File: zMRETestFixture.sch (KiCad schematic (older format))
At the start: 210 parts, among them J1 Conn_01x01, J10 Conn_01x01, J11 Conn_01x01, J2 Conn_01x01, J3 Conn_01x01_Female, J4 Conn_01x01_Female, J5 Conn_01x01, J6 Conn_01x01, J7 Conn_01x01, J8 Conn_01x01, J9 Conn_02x05_Counter_Clockwise, SW1 SW_Push, SW2 SW_Push, U1 molex_48pin_MRE

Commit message: Updated https://github.com/rusefi/hw_microRusEfi/issues/163
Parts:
- removed R57: 5k, rusefi_lib:SM0805_jumper, symbol Device:R
- removed R59: 470k, rusefi_lib:SM0805_jumper, symbol Device:R
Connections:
- wire segments 303 -> 302
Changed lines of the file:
@@
 Wire Wire Line
 	5900 2575 5900 1575
-Text Label 10725 2600 2    60   ~ 12
-5V1
-Text Label 10675 1500 2    60   ~ 12
-5V2
 Wire Wire Line
 	11525 2600 11625 2600
-$Comp
-L Device:R R59
-U 1 1 5F5B6BED
-P 11625 1650
-F 0 "R59" V 11725 1575 50  0000 L CNN
-F 1 "470k" V 11625 1650 50  0000 C CNN
-F 2 "rusefi_lib:SM0805_jumper" V 11555 1650 50  0001 C CNN
-F 3 "~" H 11625 1650 50  0001 C CNN
-F 4 "" H 3300 -4275 50  0001 C CNN "Manufacturer"
-F 5 "" H 3300 -4275 50  0001 C CNN "Part #"
-F 6 "" H 3300 -4275 50  0001 C CNN "VEND"
-F 7 "" H 3300 -4275 50  0001 C CNN "VEND#"
-F 8 "C17709" H 11625 1650 50  0001 C CNN "LCSC"
-	1    11625 1650
-	-1   0    0    1
-$EndComp
 $Comp
 L power:GND #PWR07
 U 1 1 5F5B882A
-P 11625 1875
-F 0 "#PWR07" H 11625 1625 50  0001 C CNN
-F 1 "GND" H 11630 1702 50  0000 C CNN
-F 2 "" H 11625 1875 50  0001 C CNN
-F 3 "" H 11625 1875 50  0001 C CNN
-	1    11625 1875
+P 11075 1575
+F 0 "#PWR07" H 11075 1325 50  0001 C CNN
+F 1 "GND" H 11080 1402 50  0000 C CNN
+F 2 "" H 11075 1575 50  0001 C CNN
+F 3 "" H 11075 1575 50  0001 C CNN
+	1    11075 1575
 	1    0    0    -1
 $EndComp
 Text Label 11625 1500 0    60   ~ 12
 CAM_SENSOR
-Wire Wire Line
-	10825 2600 10725 2600
-Wire Wire Line
-	10775 1500 10675 1500
 Wire Wire Line
 	9550 1575 9550 1950
@@
 Connection ~ 6425 5225
 Wire Wire Line
-	11625 1800 11625 1875
+	11075 1500 11075 1575
 Wire Wire Line
 	11625 1500 11475 1500
-Connection ~ 11625 1500
-$Comp
-L Device:R R60
-U 1 1 5F8A0C67
-P 11625 2750
-F 0 "R60" V 11725 2675 50  0000 L CNN
-F 1 "470k" V 11625 2750 50  0000 C CNN
-F 2 "rusefi_lib:SM0805_jumper" V 11555 2750 50  0001 C CNN
-F 3 "~" H 11625 2750 50  0001 C CNN
-F 4 "" H 3300 -3175 50  0001 C CNN "Manufacturer"
-F 5 "" H 3300 -3175 50  0001 C CNN "Part #"
-F 6 "" H 3300 -3175 50  0001 C CNN "VEND"
-F 7 "" H 3300 -3175 50  0001 C CNN "VEND#"
-F 8 "C17709" H 11625 2750 50  0001 C CNN "LCSC"
-	1    11625 2750
-	-1   0    0    1
-$EndComp
-$Comp
-L power:GND #PWR08
-U 1 1 5F8A5FD9
-P 11625 2975
-F 0 "#PWR08" H 11625 2725 50  0001 C CNN
-F 1 "GND" H 11630 2802 50  0000 C CNN
-F 2 "" H 11625 2975 50  0001 C CNN
-F 3 "" H 11625 2975 50  0001 C CNN
-	1    11625 2975
-	1    0    0    -1
-$EndComp
-Wire Wire Line
-	11625 2900 11625 2975
-Connection ~ 11625 2600
 Text Label 11625 2600 0    60   ~ 12
 CRNK+
-$Comp
-L Device:R R58
-U 1 1 5F96A20E
-P 10975 2600
-F 0 "R58" V 11025 2725 50  0000 L CNN
-F 1 "5k" V 10975 2600 50  0000 C CNN
-F 2 "rusefi_lib:SM0805_jumper" V 10905 2600 50  0001 C CNN
-F 3 "~" H 10975 2600 50  0001 C CNN
-F 4 "" H 2650 -3325 50  0001 C CNN "Manufacturer"
-F 5 "" H 2650 -3325 50  0001 C CNN "Part #"
-F 6 "" H 2650 -3325 50  0001 C CNN "VEND"
-F 7 "" H 2650 -3325 50  0001 C CNN "VEND#"
-F 8 "C17677" H 10975 2600 50  0001 C CNN "LCSC"
-	1    10975 2600
-	0    -1   1    0
-$EndComp
-$Comp
-L Device:R R57
-U 1 1 5F9948F0
-P 10925 1500
-F 0 "R57" V 10975 1625 50  0000 L CNN
-F 1 "5k" V 10925 1500 50  0000 C CNN
-F 2 "rusefi_lib:SM0805_jumper" V 10855 1500 50  0001 C CNN
-F 3 "~" H 10925 1500 50  0001 C CNN
-F 4 "" H 2600 -4425 50  0001 C CNN "Manufacturer"
-F 5 "" H 2600 -4425 50  0001 C CNN "Part #"
-F 6 "" H 2600 -4425 50  0001 C CNN "VEND"
-F 7 "" H 2600 -4425 50  0001 C CNN "VEND#"
-F 8 "C17677" H 10925 1500 50  0001 C CNN "LCSC"
-	1    10925 1500
-	0    -1   1    0
-$EndComp
 $Comp
 L Connector:Conn_01x01_Female J3
@@
 	0    1    1    0
 $EndComp
+Wire Wire Line
+	11625 2900 11625 2975
+$Comp
+L power:GND #PWR08
+U 1 1 5F8A5FD9
+P 11625 2975
+F 0 "#PWR08" H 11625 2725 50  0001 C CNN
+F 1 "GND" H 11630 2802 50  0000 C CNN
+F 2 "" H 11625 2975 50  0001 C CNN
+F 3 "" H 11625 2975 50  0001 C CNN
+	1    11625 2975
+	1    0    0    -1
+$EndComp
+Connection ~ 11625 2600
+$Comp
+L Device:R R60
+U 1 1 5F8A0C67
+P 11625 2750
+F 0 "R60" V 11725 2675 50  0000 L CNN
+F 1 "470k" V 11625 2750 50  0000 C CNN
+F 2 "rusefi_lib:SM0805_jumper" V 11555 2750 50  0001 C CNN
+F 3 "~" H 11625 2750 50  0001 C CNN
+F 4 "" H 3300 -3175 50  0001 C CNN "Manufacturer"
+F 5 "" H 3300 -3175 50  0001 C CNN "Part #"
+F 6 "" H 3300 -3175 50  0001 C CNN "VEND"
+F 7 "" H 3300 -3175 50  0001 C CNN "VEND#"
+F 8 "C17709" H 11625 2750 50  0001 C CNN "LCSC"
+	1    11625 2750
+	-1   0    0    1
+$EndComp
+Wire Wire Line
+	10825 2600 10725 2600
+Text Label 10725 2600 2    60   ~ 12
+5V1
+$Comp
+L Device:R R58
+U 1 1 5F96A20E
+P 10975 2600
+F 0 "R58" V 11025 2725 50  0000 L CNN
+F 1 "5k" V 10975 2600 50  0000 C CNN
+F 2 "rusefi_lib:SM0805_jumper" V 10905 2600 50  0001 C CNN
+F 3 "~" H 10975 2600 50  0001 C CNN
+F 4 "" H 2650 -3325 50  0001 C CNN "Manufacturer"
+F 5 "" H 2650 -3325 50  0001 C CNN "Part #"
+F 6 "" H 2650 -3325 50  0001 C CNN "VEND"
+F 7 "" H 2650 -3325 50  0001 C CNN "VEND#"
+F 8 "C17677" H 10975 2600 50  0001 C CNN "LCSC"
+	1    10975 2600
+	0    -1   1    0
+$EndComp
 $EndSCHEMATC

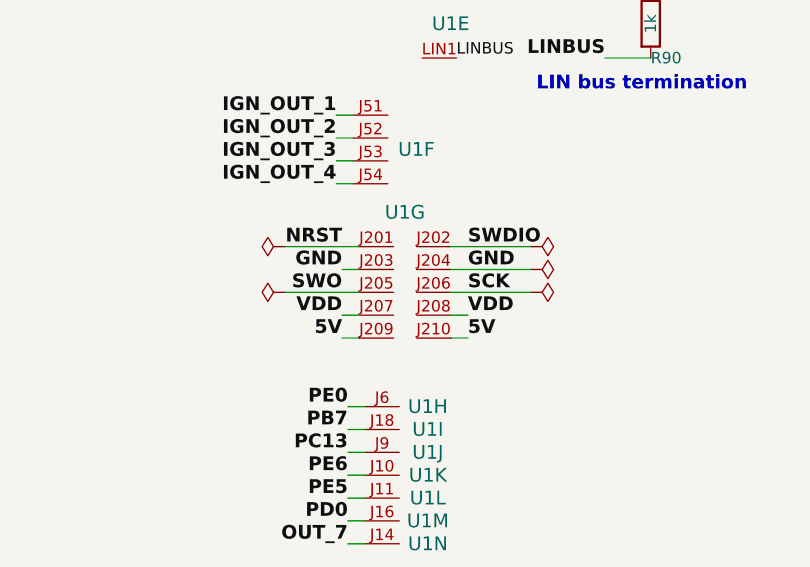
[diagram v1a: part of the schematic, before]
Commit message: Fixed flipped J2 per https://github.com/rusefi/hw_microRusEfi/issues/179
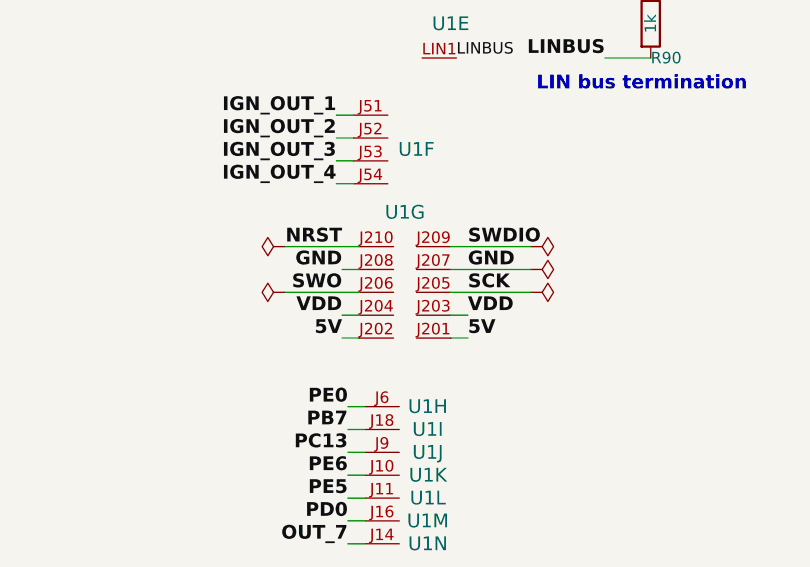
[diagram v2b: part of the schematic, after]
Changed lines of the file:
@@
 Sheet 1 1
 Title "zMRETestFixture"
-Date "2020-05-14"
-Rev "R0.1"
+Date "2020-07-08"
+Rev "R0.2"
 Comp "rusEFI.com"
 Comment1 ""
@@
 L rusefi_Molex_MRE_Connector:molex_48pin_MRE U1
 U 7 1 5EE5179C
-P 13825 3900
-F 0 "U1" H 14725 4250 60  0000 C CNN
-F 1 "molex_48pin_MRE" V 15006 4305 60  0001 C CNN
-F 2 "rusefi_lib:Molex_48_MRE" H 13825 3900 60  0001 C CNN
-F 3 "" H 13825 3900 60  0001 C CNN
-F 4 "MOLEX" H 6075 1775 50  0001 C CNN "Manufacturer"
-F 5 "500762-0481" H 6075 1775 50  0001 C CNN "Part #"
-F 6 "DIGI" H 6075 1775 50  0001 C CNN "VEND"
-F 7 "WM4430-ND" H 6075 1775 50  0001 C CNN "VEND#"
-	7    13825 3900
-	1    0    0    -1
-$EndComp
-$Comp
+P 15625 3900
+F 0 "U1" H 16525 3550 60  0000 C CNN
+F 1 "molex_48pin_MRE" V 16806 4305 60  0001 C CNN
+F 2 "rusefi_lib:Molex_48_MRE" H 15625 3900 60  0001 C CNN
+F 3 "" H 15625 3900 60  0001 C CNN
+F 4 "MOLEX" H 7875 1775 50  0001 C CNN "Manufacturer"
+F 5 "500762-0481" H 7875 1775 50  0001 C CNN "Part #"
+F 6 "DIGI" H 7875 1775 50  0001 C CNN "VEND"
+F 7 "WM4430-ND" H 7875 1775 50  0001 C CNN "VEND#"
+	7    15625 3900
+	-1   0    0    1
+$EndComp
+$Comp

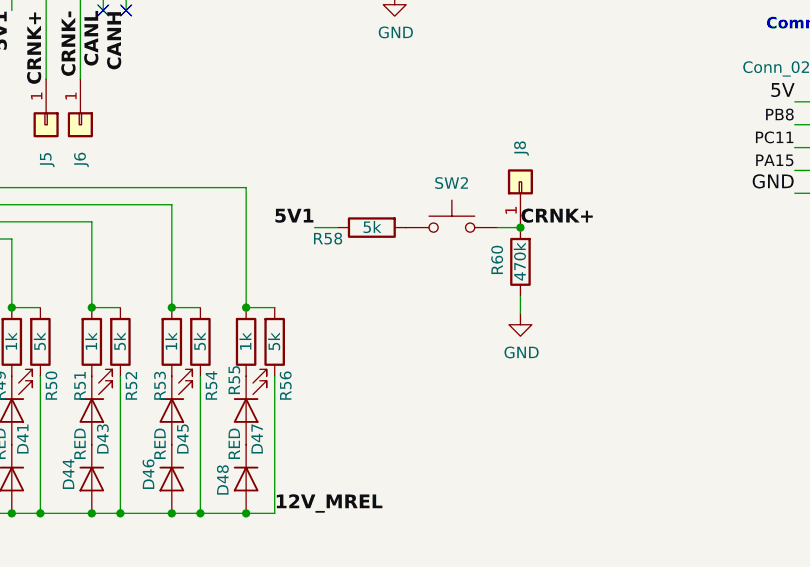
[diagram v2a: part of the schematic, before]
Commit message: Bumped silk to to R0.2 and changed CRANK per https://github.com/rusefi/hw_microRusEfi/issues/177
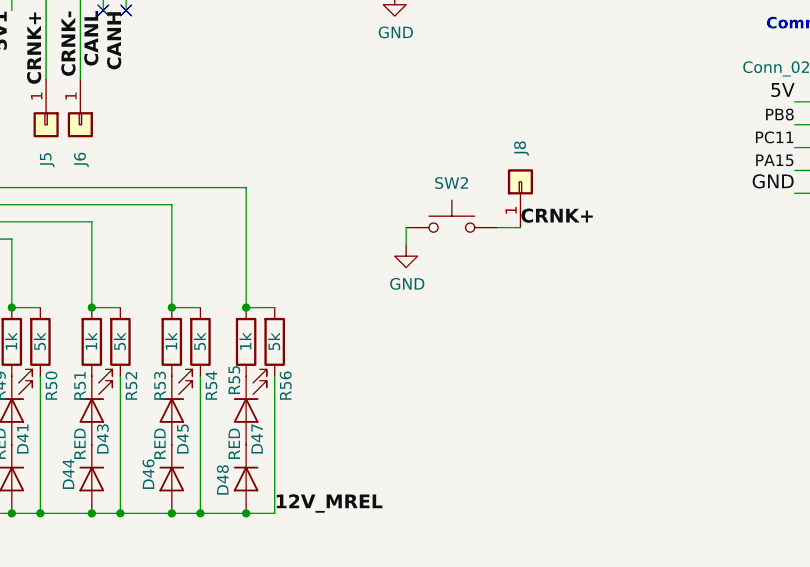
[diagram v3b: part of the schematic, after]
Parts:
- removed R58: 5k, rusefi_lib:SM0805_jumper, symbol Device:R
- removed R60: 470k, rusefi_lib:SM0805_jumper, symbol Device:R
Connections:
- wire segments 302 -> 301
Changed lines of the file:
@@
 $EndComp
 Wire Wire Line
-	11625 2900 11625 2975
+	11125 2600 11125 2675
 $Comp
 L power:GND #PWR08
 U 1 1 5F8A5FD9
-P 11625 2975
-F 0 "#PWR08" H 11625 2725 50  0001 C CNN
-F 1 "GND" H 11630 2802 50  0000 C CNN
-F 2 "" H 11625 2975 50  0001 C CNN
-F 3 "" H 11625 2975 50  0001 C CNN
-	1    11625 2975
+P 11125 2675
+F 0 "#PWR08" H 11125 2425 50  0001 C CNN
+F 1 "GND" H 11130 2502 50  0000 C CNN
+F 2 "" H 11125 2675 50  0001 C CNN
+F 3 "" H 11125 2675 50  0001 C CNN
+	1    11125 2675
 	1    0    0    -1
 $EndComp
-Connection ~ 11625 2600
-$Comp
-L Device:R R60
-U 1 1 5F8A0C67
-P 11625 2750
-F 0 "R60" V 11725 2675 50  0000 L CNN
-F 1 "470k" V 11625 2750 50  0000 C CNN
-F 2 "rusefi_lib:SM0805_jumper" V 11555 2750 50  0001 C CNN
-F 3 "~" H 11625 2750 50  0001 C CNN
-F 4 "" H 3300 -3175 50  0001 C CNN "Manufacturer"
-F 5 "" H 3300 -3175 50  0001 C CNN "Part #"
-F 6 "" H 3300 -3175 50  0001 C CNN "VEND"
-F 7 "" H 3300 -3175 50  0001 C CNN "VEND#"
-F 8 "C17709" H 11625 2750 50  0001 C CNN "LCSC"
-	1    11625 2750
-	-1   0    0    1
-$EndComp
-Wire Wire Line
-	10825 2600 10725 2600
-Text Label 10725 2600 2    60   ~ 12
-5V1
-$Comp
-L Device:R R58
-U 1 1 5F96A20E
-P 10975 2600
-F 0 "R58" V 11025 2725 50  0000 L CNN
-F 1 "5k" V 10975 2600 50  0000 C CNN
-F 2 "rusefi_lib:SM0805_jumper" V 10905 2600 50  0001 C CNN
-F 3 "~" H 10975 2600 50  0001 C CNN
-F 4 "" H 2650 -3325 50  0001 C CNN "Manufacturer"
-F 5 "" H 2650 -3325 50  0001 C CNN "Part #"
-F 6 "" H 2650 -3325 50  0001 C CNN "VEND"
-F 7 "" H 2650 -3325 50  0001 C CNN "VEND#"
-F 8 "C17677" H 10975 2600 50  0001 C CNN "LCSC"
-	1    10975 2600
-	0    -1   1    0
-$EndComp
 $EndSCHEMATC
